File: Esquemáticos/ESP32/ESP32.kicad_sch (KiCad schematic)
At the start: 1 part

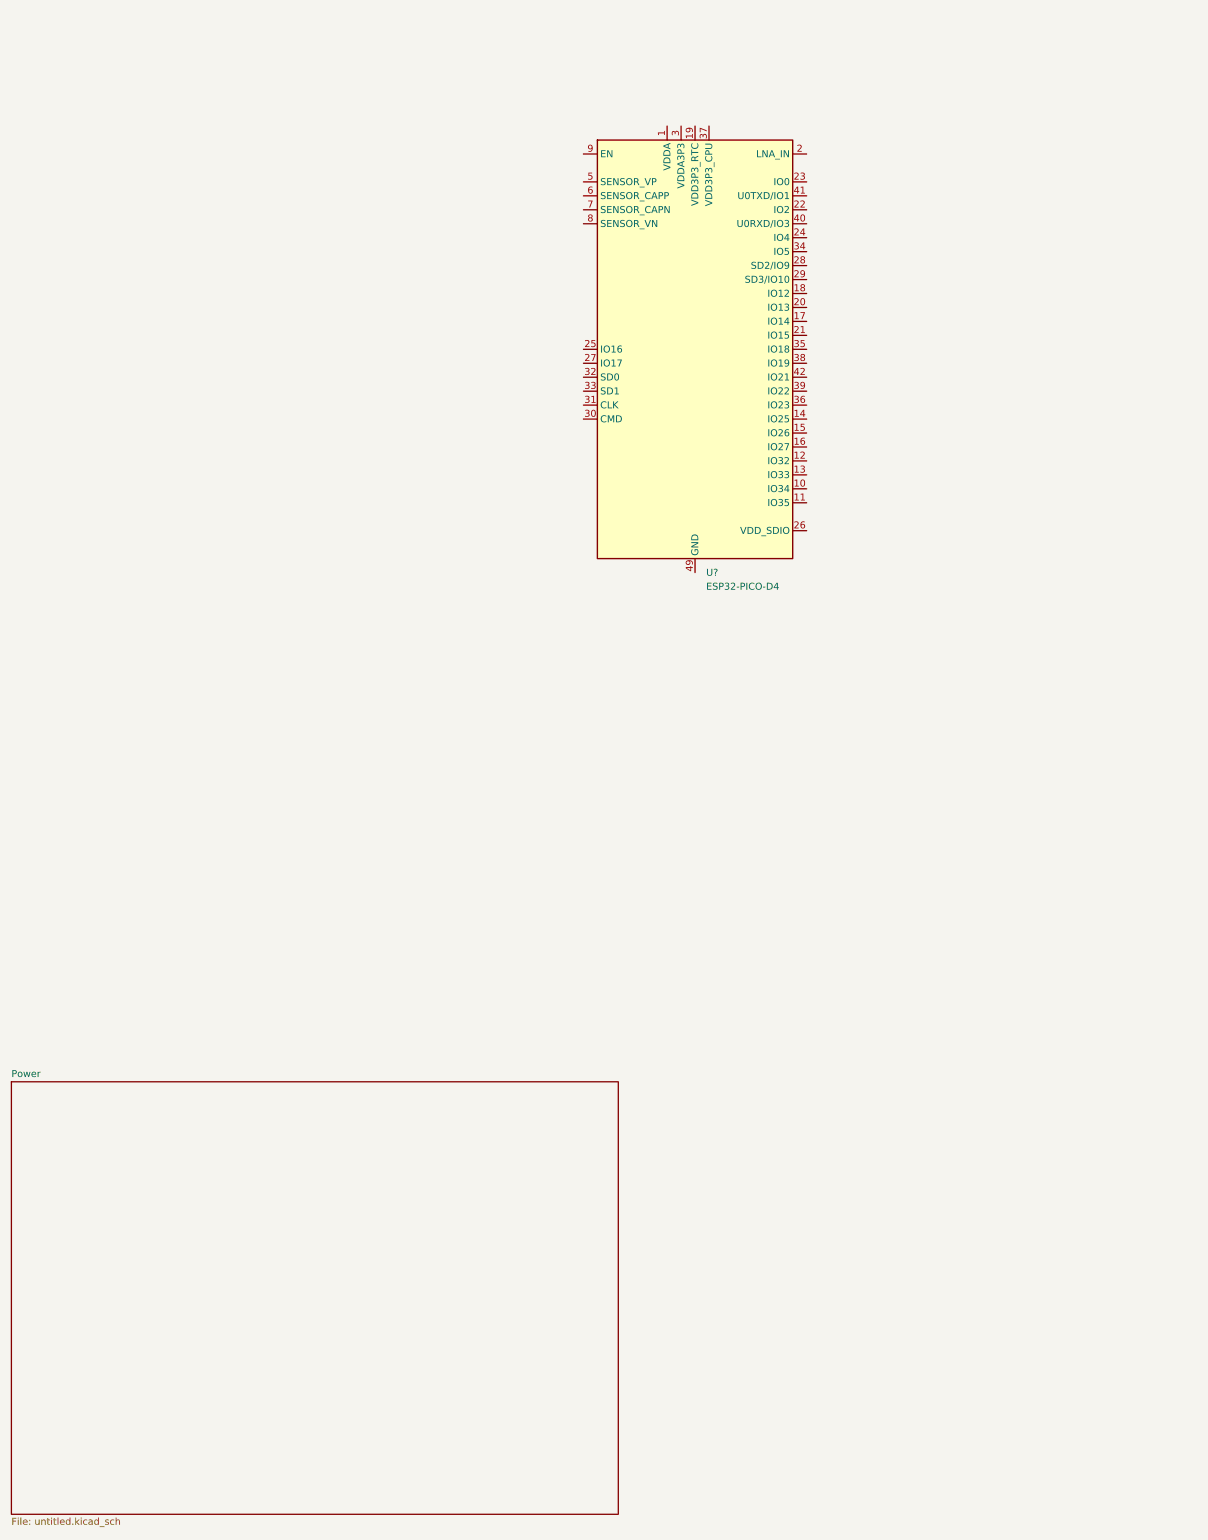
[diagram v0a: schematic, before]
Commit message: Agregada la parte de motores a la jerarquía de esquemáticos
:+1:
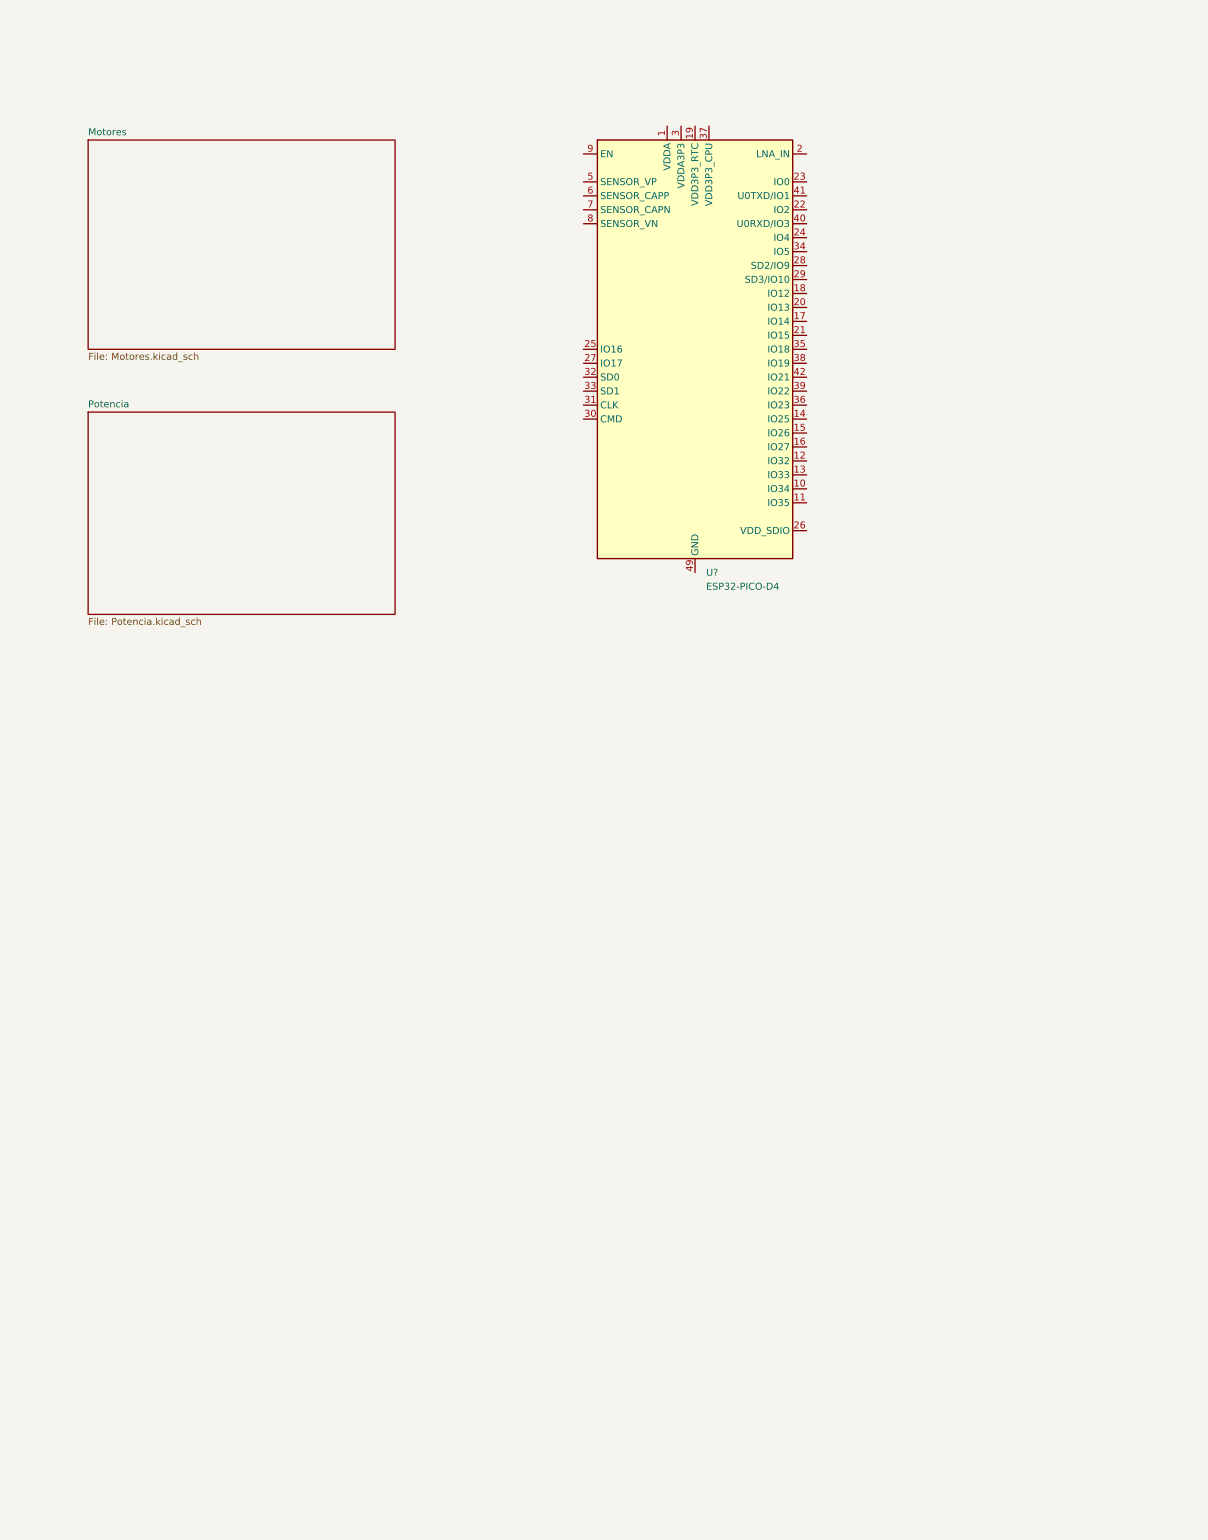
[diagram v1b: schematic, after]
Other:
- sheet Power renamed Potencia
- added sheet Motores (Motores.kicad_sch)
- sheet Potencia: file untitled.kicad_sch -> Potencia.kicad_sch
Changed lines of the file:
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@@
     (pin "9")
   )
-  (sheet (at 20.32 233.68) (size 110.49 78.74) (fields_autoplaced)
+  (sheet (at 34.29 111.76) (size 55.88 36.83) (fields_autoplaced)
     (stroke (width 0.1524) (type solid) (color 0 0 0 0))
     (fill (color 0 0 0 0.0000))
-    (property "Sheet name" "Power" (id 0) (at 20.32 232.9684 0)
+    (property "Sheet name" "Potencia" (id 0) (at 34.29 111.0484 0)
       (effects (font (size 1.27 1.27)) (justify left bottom))
     )
-    (property "Sheet file" "untitled.kicad_sch" (id 1) (at 20.32 313.0046 0)
+    (property "Sheet file" "Potencia.kicad_sch" (id 1) (at 34.29 149.1746 0)
+      (effects (font (size 1.27 1.27)) (justify left top))
+    )
+  )
+  (sheet (at 34.29 62.23) (size 55.88 38.1) (fields_autoplaced)
+    (stroke (width 0.1524) (type solid) (color 0 0 0 0))
+    (fill (color 0 0 0 0.0000))
+    (property "Sheet name" "Motores" (id 0) (at 34.29 61.5184 0)
+      (effects (font (size 1.27 1.27)) (justify left bottom))
+    )
+    (property "Sheet file" "Motores.kicad_sch" (id 1) (at 34.29 100.9146 0)
       (effects (font (size 1.27 1.27)) (justify left top))
     )
@@
     (path "/" (page "1"))
     (path "/3dc66758-7067-4285-a03f-e9474bf12d83" (page "2"))
+    (path "/e1e74fdb-71e2-41d9-bc36-66c7a8ec4b6a" (page "3"))
   )
   (symbol_instances
@@
       (reference "#PWR?") (unit 1) (value "GND") (footprint "")
     )
+    (path "/e1e74fdb-71e2-41d9-bc36-66c7a8ec4b6a/333834cc-7b59-4d57-9ac5-bddc65fce3e3"
+      (reference "#PWR?") (unit 1) (value "GND") (footprint "")
+    )
     (path "/3dc66758-7067-4285-a03f-e9474bf12d83/621ff814-a68f-4bb5-8279-ead22c61f352"
       (reference "#PWR?") (unit 1) (value "GND") (footprint "")
     )
     (path "/3dc66758-7067-4285-a03f-e9474bf12d83/6334ead4-e783-4de0-a428-c9983f3bd26d"
+      (reference "#PWR?") (unit 1) (value "GND") (footprint "")
+    )
+    (path "/e1e74fdb-71e2-41d9-bc36-66c7a8ec4b6a/7108ffff-73e3-45ac-9eef-ceb75d463b34"
       (reference "#PWR?") (unit 1) (value "GND") (footprint "")
     )
@@
       (reference "#PWR?") (unit 1) (value "Earth") (footprint "")
     )
+    (path "/e1e74fdb-71e2-41d9-bc36-66c7a8ec4b6a/b637b42a-cfe5-431d-9fdd-04c64c112d71"
+      (reference "#PWR?") (unit 1) (value "GND") (footprint "")
+    )
+    (path "/e1e74fdb-71e2-41d9-bc36-66c7a8ec4b6a/cb0a6283-864c-4112-88a1-3cc92469d704"
+      (reference "#PWR?") (unit 1) (value "GND") (footprint "")
+    )
+    (path "/e1e74fdb-71e2-41d9-bc36-66c7a8ec4b6a/d9b8169f-cf1d-4fd2-807f-95aa153c2a53"
+      (reference "#PWR?") (unit 1) (value "GND") (footprint "")
+    )
     (path "/3dc66758-7067-4285-a03f-e9474bf12d83/e56ebd87-4171-43b6-8b3c-3a8f71003486"
       (reference "#PWR?") (unit 1) (value "GND") (footprint "")
+    )
+    (path "/e1e74fdb-71e2-41d9-bc36-66c7a8ec4b6a/3cfbb91b-3697-49dc-9cc5-7f20a0dde55d"
+      (reference "C1") (unit 1) (value "100n") (footprint "")
     )
     (path "/3dc66758-7067-4285-a03f-e9474bf12d83/785de56d-3c47-406a-aa51-0e72d54be645"
@@
     (path "/3dc66758-7067-4285-a03f-e9474bf12d83/be1a9dce-3027-4f1e-9027-6127298a03b0"
       (reference "C2") (unit 1) (value "1000uF") (footprint "")
+    )
+    (path "/e1e74fdb-71e2-41d9-bc36-66c7a8ec4b6a/cf31adad-d59f-48cc-a46c-715baccd87a3"
+      (reference "C2") (unit 1) (value "100n") (footprint "")
     )
     (path "/3dc66758-7067-4285-a03f-e9474bf12d83/015314e6-8f16-4659-98a6-76c6eb4804be"
@@
       (reference "D?") (unit 1) (value "BZT52Bxx") (footprint "Diode_SMD:D_SOD-123F")
     )
+    (path "/e1e74fdb-71e2-41d9-bc36-66c7a8ec4b6a/dd873b04-eead-4a5d-887d-1c89c6e94b62"
+      (reference "J1") (unit 1) (value "Conector para bobinas del motor 1") (footprint "")
+    )
+    (path "/e1e74fdb-71e2-41d9-bc36-66c7a8ec4b6a/a90ebcb0-52d5-4b3f-b94a-f8cfc528c128"
+      (reference "J2") (unit 1) (value "Conector para bobinas del motor 2") (footprint "")
+    )
     (path "/3dc66758-7067-4285-a03f-e9474bf12d83/e33de0b8-310e-4c90-a1cc-6d9bb1ac1b41"
       (reference "J?") (unit 1) (value "Barrel_Jack") (footprint "")
@@
       (reference "L1") (unit 1) (value "68u") (footprint "")
     )
+    (path "/e1e74fdb-71e2-41d9-bc36-66c7a8ec4b6a/84db0748-82ca-4a29-8b2f-07b9a3e175b0"
+      (reference "Q?") (unit 1) (value "S8050") (footprint "Package_TO_SOT_THT:TO-92_Inline")
+    )
     (path "/3dc66758-7067-4285-a03f-e9474bf12d83/02b32956-838d-4e64-a5e8-7054f9afa174"
       (reference "R?") (unit 1) (value "10k") (footprint "")
+    )
+    (path "/e1e74fdb-71e2-41d9-bc36-66c7a8ec4b6a/2e492155-183b-4e1a-bc38-b02d621150a9"
+      (reference "R?") (unit 1) (value "220") (footprint "")
     )
     (path "/3dc66758-7067-4285-a03f-e9474bf12d83/379573b5-5cb0-4557-b536-5924669a1026"
       (reference "R?") (unit 1) (value "R") (footprint "")
     )
+    (path "/e1e74fdb-71e2-41d9-bc36-66c7a8ec4b6a/b324ba5f-5bc4-4ae9-8a69-e835655a8c55"
+      (reference "R?") (unit 1) (value "5.1k") (footprint "")
+    )
+    (path "/e1e74fdb-71e2-41d9-bc36-66c7a8ec4b6a/c6ee4151-94ac-4f32-97d1-bc916978f4bc"
+      (reference "R?") (unit 1) (value "5.1k") (footprint "")
+    )
     (path "/3dc66758-7067-4285-a03f-e9474bf12d83/86731196-21f1-42f1-830f-08ae7cbba978"
       (reference "SW?") (unit 1) (value "SW_DIP_x01") (footprint "")
     )
+    (path "/e1e74fdb-71e2-41d9-bc36-66c7a8ec4b6a/5bf74cd1-a962-4bbd-9f53-d2bee3f6a861"
+      (reference "U1") (unit 1) (value "ULN2003A") (footprint "")
+    )
     (path "/3dc66758-7067-4285-a03f-e9474bf12d83/d1a67861-4cc5-42f5-82d1-2c6abe3b244f"
       (reference "U1") (unit 1) (value "LM2596S-5") (footprint "Package_TO_SOT_SMD:TO-263-5_TabPin3")
+    )
+    (path "/e1e74fdb-71e2-41d9-bc36-66c7a8ec4b6a/5d1e4c1d-d89f-4fb1-bada-7233db96a26f"
+      (reference "U2") (unit 1) (value "ULN2003A") (footprint "")
     )
     (path "/266e158e-7474-4de0-b2cb-c3efc5bc9c58"
@@
       (reference "U?") (unit 1) (value "AMS1117-3.3") (footprint "Package_TO_SOT_SMD:SOT-223-3_TabPin2")
     )
+    (path "/e1e74fdb-71e2-41d9-bc36-66c7a8ec4b6a/f7965755-6f1a-4b02-9c6c-4500de9fac77"
+      (reference "U?") (unit 1) (value "LTV-247") (footprint "Package_SO:SOP-16_4.4x10.4mm_P1.27mm")
+    )
   )

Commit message: mensaje
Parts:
- removed U?: ESP32-PICO-D4, Package_DFN_QFN:QFN-48-1EP_7x7mm_P0.5mm_EP5.3x5.3mm, symbol RF_Module:ESP32-PICO-D4
- added U?: ESP32-WROOM-32, RF_Module:ESP32-WROOM-32, symbol RF_Module:ESP32-WROOM-32
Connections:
- new net 3.3V: U?.2 (VDD)
- new net GND: U?.1 (GND), U?.15 (GND), U?.38 (GND), U?.39 (GND)
- new net MISO: U?.31 (IO19)
- new net MOSI: U?.37 (IO23)
- new net RST: U?.36 (IO22)
- new net SCK: U?.30 (IO18)
- new net SS: U?.29 (IO5)
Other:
- added sheet RFID (RFID.kicad_sch)
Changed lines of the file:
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@@
 (kicad_sch (version 20211123) (generator eeschema)
   (paper "A4")
-  (symbol (lib_id "RF_Module:ESP32-PICO-D4") (at 144.78 100.33 0) (unit 1)
+  (global_label "GND" (shape input) (at 140.97 125.73 270) (fields_autoplaced)
+    (effects (font (size 1.27 1.27)) (justify right))
+    (property "Referencias entre hojas" "${INTERSHEET_REFS}" (id 0) (at 140.8906 132.0136 90)
+      (effects (font (size 1.27 1.27)) (justify right) hide)
+    )
+  )
+  (global_label "3.3V" (shape input) (at 140.97 54.61 90) (fields_autoplaced)
+    (effects (font (size 1.27 1.27)) (justify left))
+    (property "Referencias entre hojas" "${INTERSHEET_REFS}" (id 0) (at 140.8906 48.0845 90)
+      (effects (font (size 1.27 1.27)) (justify left) hide)
+    )
+  )
+  (global_label "MISO" (shape input) (at 156.21 92.71 0) (fields_autoplaced)
+    (effects (font (size 1.27 1.27)) (justify left))
+    (property "Referencias entre hojas" "${INTERSHEET_REFS}" (id 0) (at 163.2193 92.6306 0)
+      (effects (font (size 1.27 1.27)) (justify left) hide)
+    )
+  )
+  (global_label "SCK" (shape input) (at 156.21 90.17 0) (fields_autoplaced)
+    (effects (font (size 1.27 1.27)) (justify left))
+    (property "Referencias entre hojas" "${INTERSHEET_REFS}" (id 0) (at 162.3726 90.0906 0)
+      (effects (font (size 1.27 1.27)) (justify left) hide)
+    )
+  )
+  (global_label "RST" (shape input) (at 156.21 97.79 0) (fields_autoplaced)
+    (effects (font (size 1.27 1.27)) (justify left))
+    (property "Referencias entre hojas" "${INTERSHEET_REFS}" (id 0) (at 162.0702 97.7106 0)
+      (effects (font (size 1.27 1.27)) (justify left) hide)
+    )
+  )
+  (global_label "SS" (shape input) (at 156.21 72.39 0) (fields_autoplaced)
+    (effects (font (size 1.27 1.27)) (justify left))
+    (property "Referencias entre hojas" "${INTERSHEET_REFS}" (id 0) (at 161.0421 72.3106 0)
+      (effects (font (size 1.27 1.27)) (justify left) hide)
+    )
+  )
+  (global_label "MOSI" (shape input) (at 156.21 100.33 0) (fields_autoplaced)
+    (effects (font (size 1.27 1.27)) (justify left))
+    (property "Referencias entre hojas" "${INTERSHEET_REFS}" (id 0) (at 163.2193 100.2506 0)
+      (effects (font (size 1.27 1.27)) (justify left) hide)
+    )
+  )
+  (symbol (lib_id "RF_Module:ESP32-WROOM-32") (at 140.97 90.17 0) (unit 1)
     (in_bom yes) (on_board yes) (fields_autoplaced)
-    (property "Reference" "U?" (id 0) (at 146.7994 140.97 0)
+    (property "Reference" "U?" (id 0) (at 142.9894 52.07 0)
       (effects (font (size 1.27 1.27)) (justify left))
     )
-    (property "Value" "ESP32-PICO-D4" (id 1) (at 146.7994 143.51 0)
+    (property "Value" "ESP32-WROOM-32" (id 1) (at 142.9894 54.61 0)
       (effects (font (size 1.27 1.27)) (justify left))
     )
-    (property "Footprint" "Package_DFN_QFN:QFN-48-1EP_7x7mm_P0.5mm_EP5.3x5.3mm" (id 2) (at 144.78 143.51 0)
+    (property "Footprint" "RF_Module:ESP32-WROOM-32" (id 2) (at 140.97 128.27 0)
       (effects (font (size 1.27 1.27)) hide)
     )
-    (property "Datasheet" "https://www.espressif.com/sites/default/files/documentation/esp32-pico-d4_datasheet_en.pdf" (id 3) (at 151.13 125.73 0)
+    (property "Datasheet" "https://www.espressif.com/sites/default/files/documentation/esp32-wroom-32_datasheet_en.pdf" (id 3) (at 133.35 88.9 0)
       (effects (font (size 1.27 1.27)) hide)
     )
@@
     (pin "39")
     (pin "4")
-    (pin "40")
-    (pin "41")
-    (pin "42")
-    (pin "43")
-    (pin "44")
-    (pin "45")
-    (pin "46")
-    (pin "47")
-    (pin "48")
-    (pin "49")
     (pin "5")
     (pin "6")
@@
     )
   )
+  (sheet (at 184.15 73.66) (size 12.7 31.75) (fields_autoplaced)
+    (stroke (width 0.1524) (type solid) (color 0 0 0 0))
+    (fill (color 0 0 0 0.0000))
+    (property "Sheet name" "RFID" (id 0) (at 184.15 72.9484 0)
+      (effects (font (size 1.27 1.27)) (justify left bottom))
+    )
+    (property "Sheet file" "RFID.kicad_sch" (id 1) (at 184.15 105.9946 0)
+      (effects (font (size 1.27 1.27)) (justify left top))
+    )
+  )
   (sheet (at 34.29 62.23) (size 55.88 38.1) (fields_autoplaced)
     (stroke (width 0.1524) (type solid) (color 0 0 0 0))
@@
     (path "/3dc66758-7067-4285-a03f-e9474bf12d83" (page "2"))
     (path "/e1e74fdb-71e2-41d9-bc36-66c7a8ec4b6a" (page "3"))
+    (path "/80dbd6db-b9cc-42d5-a40e-8d2c99f93a1b" (page "4"))
   )
   (symbol_instances
@@
       (reference "J2") (unit 1) (value "Conector para bobinas del motor 2") (footprint "")
     )
+    (path "/80dbd6db-b9cc-42d5-a40e-8d2c99f93a1b/3471c47f-a636-4058-83f1-2e9cb217714f"
+      (reference "J?") (unit 1) (value "Conn_RFID_SPI") (footprint "")
+    )
     (path "/3dc66758-7067-4285-a03f-e9474bf12d83/e33de0b8-310e-4c90-a1cc-6d9bb1ac1b41"
       (reference "J?") (unit 1) (value "Barrel_Jack") (footprint "")
@@
       (reference "U2") (unit 1) (value "ULN2003A") (footprint "")
     )
-    (path "/266e158e-7474-4de0-b2cb-c3efc5bc9c58"
-      (reference "U?") (unit 1) (value "ESP32-PICO-D4") (footprint "Package_DFN_QFN:QFN-48-1EP_7x7mm_P0.5mm_EP5.3x5.3mm")
-    )
     (path "/3dc66758-7067-4285-a03f-e9474bf12d83/43b937ef-b7e6-4e46-9361-ca0038217fbd"
       (reference "U?") (unit 1) (value "AMS1117-3.3") (footprint "Package_TO_SOT_SMD:SOT-223-3_TabPin2")
     )
+    (path "/7126fc01-b23f-49c1-b635-013e178bb3de"
+      (reference "U?") (unit 1) (value "ESP32-WROOM-32") (footprint "RF_Module:ESP32-WROOM-32")
+    )
     (path "/e1e74fdb-71e2-41d9-bc36-66c7a8ec4b6a/f7965755-6f1a-4b02-9c6c-4500de9fac77"
